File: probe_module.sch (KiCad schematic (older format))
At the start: 4 parts, among them J6 CONN_01X05, J7 CONN_01X05, U6 DG411, U7 LH1526

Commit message: Re-annotation
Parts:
- removed unit 1 of U6
- removed unit 3 of U6
- removed unit 4 of U6
- removed U7: LH1526, symbol LH1526
- added unit 1 of U5
- added unit 3 of U5
- added unit 4 of U5
- added U6: LH1526, symbol LH1526
- renumbered U6 to U5
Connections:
- net +3V3: now also U5.13 (V+), U5.13 (V+), U5.13 (V+)
- net GND: now also U5.4 (V-), U5.4 (V-), U5.4 (V-), U5.5 (GND), U5.5 (GND), U5.5 (GND), U6.2 (CTRL1_out), U6.4 (CTRL2_out)
- net VCC: now also U5.12 (VCC), U5.12 (VCC), U5.12 (VCC), U6.6 (S2), U6.8 (S1)
- net prb1_a: now also U5.3 (OUT)
- net prb1_pwr_ctrl: now also U6.1 (CTRL1_in)
- net prb1_rs_ctrl: now also U5.1 (SW)
- net prb1_v: now also U6.5 (S2')
- net prb2_a: now also U5.11 (OUT)
- net prb2_b: now also U5.15 (IN)
- net prb2_pwr_ctrl: now also U6.3 (CTRL2_in)
- net prb2_rs_ctrl: now also U5.16 (SW), U5.9 (SW)
- net prb2_v: now also U6.7 (S1')
- net vaisala_rs485_a: now also U5.10 (IN), U5.2 (IN)
- net vaisala_rs485_b: now also U5.14 (OUT)
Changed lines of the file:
@@
 $EndDescr
 $Comp
-L DG411 U6
-U 1 1 5981A21D
+L DG411 U5
+U 1 1 59945E5C
 P 2300 4450
-AR Path="/598183C5/5981A21D" Ref="U6"  Part="1"
-AR Path="/59933B07/5981A21D" Ref="U10"  Part="1"
-F 0 "U6" H 2300 4550 50  0000 C CNN
+F 0 "U5" H 2300 4550 50  0000 C CNN
 F 1 "DG411" H 2300 4350 50  0000 C CNN
 F 2 "" H 2300 4450 60  0001 C CNN
@@
 $EndComp
 $Comp
-L GND #PWR041
+L GND #PWR35
 U 1 1 5981A4AC
 P 2350 4950
-AR Path="/598183C5/5981A4AC" Ref="#PWR041"  Part="1"
-AR Path="/59933B07/5981A4AC" Ref="#PWR95"  Part="1"
-F 0 "#PWR041" H 2350 4700 50  0001 C CNN
+F 0 "#PWR35" H 2350 4700 50  0001 C CNN
 F 1 "GND" H 2350 4800 50  0000 C CNN
 F 2 "" H 2350 4950 50  0001 C CNN
@@
 $EndComp
 $Comp
-L GND #PWR042
+L GND #PWR38
 U 1 1 5981A5BD
 P 4700 4950
-AR Path="/598183C5/5981A5BD" Ref="#PWR042"  Part="1"
-AR Path="/59933B07/5981A5BD" Ref="#PWR98"  Part="1"
-F 0 "#PWR042" H 4700 4700 50  0001 C CNN
+F 0 "#PWR38" H 4700 4700 50  0001 C CNN
 F 1 "GND" H 4700 4800 50  0000 C CNN
 F 2 "" H 4700 4950 50  0001 C CNN
@@
 $EndComp
 $Comp
-L +3.3V #PWR043
+L +3.3V #PWR34
 U 1 1 5981A680
 P 2350 3950
-AR Path="/598183C5/5981A680" Ref="#PWR043"  Part="1"
-AR Path="/59933B07/5981A680" Ref="#PWR94"  Part="1"
-F 0 "#PWR043" H 2350 3800 50  0001 C CNN
+F 0 "#PWR34" H 2350 3800 50  0001 C CNN
 F 1 "+3.3V" H 2350 4090 50  0000 C CNN
 F 2 "" H 2350 3950 50  0001 C CNN
@@
 $EndComp
 $Comp
-L +3.3V #PWR044
+L +3.3V #PWR37
 U 1 1 5981A69E
 P 4700 3950
-AR Path="/598183C5/5981A69E" Ref="#PWR044"  Part="1"
-AR Path="/59933B07/5981A69E" Ref="#PWR97"  Part="1"
-F 0 "#PWR044" H 4700 3800 50  0001 C CNN
+F 0 "#PWR37" H 4700 3800 50  0001 C CNN
 F 1 "+3.3V" H 4700 4090 50  0000 C CNN
 F 2 "" H 4700 3950 50  0001 C CNN
@@
 prb1_b
 $Comp
-L DG411 U6
+L DG411 U5
 U 2 1 5981A26A
 P 4650 4450
-AR Path="/598183C5/5981A26A" Ref="U6"  Part="2"
-AR Path="/59933B07/5981A26A" Ref="U10"  Part="2"
-F 0 "U6" H 4650 4550 50  0000 C CNN
+F 0 "U5" H 4650 4550 50  0000 C CNN
 F 1 "DG411" H 4650 4350 50  0000 C CNN
 F 2 "" H 4650 4450 60  0001 C CNN
@@
 vaisala_rs485_b
 $Comp
-L DG411 U6
-U 3 1 5981EAC3
+L DG411 U5
+U 3 1 59945E6E
 P 7400 4450
-AR Path="/598183C5/5981EAC3" Ref="U6"  Part="3"
-AR Path="/59933B07/5981EAC3" Ref="U10"  Part="3"
-F 0 "U6" H 7400 4550 50  0000 C CNN
+F 0 "U5" H 7400 4550 50  0000 C CNN
 F 1 "DG411" H 7400 4350 50  0000 C CNN
 F 2 "" H 7400 4450 60  0001 C CNN
@@
 $EndComp
 $Comp
-L GND #PWR045
-U 1 1 5981EAC9
+L GND #PWR44
+U 1 1 59945E6F
 P 7450 4950
-AR Path="/598183C5/5981EAC9" Ref="#PWR045"  Part="1"
-AR Path="/59933B07/5981EAC9" Ref="#PWR104"  Part="1"
-F 0 "#PWR045" H 7450 4700 50  0001 C CNN
+F 0 "#PWR44" H 7450 4700 50  0001 C CNN
 F 1 "GND" H 7450 4800 50  0000 C CNN
 F 2 "" H 7450 4950 50  0001 C CNN
@@
 $EndComp
 $Comp
-L GND #PWR046
-U 1 1 5981EACF
+L GND #PWR47
+U 1 1 59945E70
 P 9500 4900
-AR Path="/598183C5/5981EACF" Ref="#PWR046"  Part="1"
-AR Path="/59933B07/5981EACF" Ref="#PWR107"  Part="1"
-F 0 "#PWR046" H 9500 4650 50  0001 C CNN
+F 0 "#PWR47" H 9500 4650 50  0001 C CNN
 F 1 "GND" H 9500 4750 50  0000 C CNN
 F 2 "" H 9500 4900 50  0001 C CNN
@@
 $EndComp
 $Comp
-L +3.3V #PWR047
-U 1 1 5981EAD5
+L +3.3V #PWR43
+U 1 1 59945E71
 P 7450 3950
-AR Path="/598183C5/5981EAD5" Ref="#PWR047"  Part="1"
-AR Path="/59933B07/5981EAD5" Ref="#PWR103"  Part="1"
-F 0 "#PWR047" H 7450 3800 50  0001 C CNN
+F 0 "#PWR43" H 7450 3800 50  0001 C CNN
 F 1 "+3.3V" H 7450 4090 50  0000 C CNN
 F 2 "" H 7450 3950 50  0001 C CNN
@@
 $EndComp
 $Comp
-L +3.3V #PWR048
-U 1 1 5981EADB
+L +3.3V #PWR46
+U 1 1 59945E72
 P 9500 3900
-AR Path="/598183C5/5981EADB" Ref="#PWR048"  Part="1"
-AR Path="/59933B07/5981EADB" Ref="#PWR106"  Part="1"
-F 0 "#PWR048" H 9500 3750 50  0001 C CNN
+F 0 "#PWR46" H 9500 3750 50  0001 C CNN
 F 1 "+3.3V" H 9500 4040 50  0000 C CNN
 F 2 "" H 9500 3900 50  0001 C CNN
@@
 prb2_b
 $Comp
-L DG411 U6
-U 4 1 5981EAE3
+L DG411 U5
+U 4 1 59945E73
 P 9450 4400
-AR Path="/598183C5/5981EAE3" Ref="U6"  Part="4"
-AR Path="/59933B07/5981EAE3" Ref="U10"  Part="4"
-F 0 "U6" H 9450 4500 50  0000 C CNN
+F 0 "U5" H 9450 4500 50  0000 C CNN
 F 1 "DG411" H 9450 4300 50  0000 C CNN
 F 2 "" H 9450 4400 60  0001 C CNN
@@
 $Comp
 L CONN_01X05 J6
-U 1 1 598215F3
+U 1 1 59945E74
 P 3100 1700
-AR Path="/598183C5/598215F3" Ref="J6"  Part="1"
-AR Path="/59933B07/598215F3" Ref="J9"  Part="1"
 F 0 "J6" H 3100 2000 50  0000 C CNN
 F 1 "CONN_01X05" V 3200 1700 50  0000 C CNN
@@
 U 1 1 59821868
 P 8000 1600
-AR Path="/598183C5/59821868" Ref="J7"  Part="1"
-AR Path="/59933B07/59821868" Ref="J10"  Part="1"
 F 0 "J7" H 8000 1900 50  0000 C CNN
 F 1 "CONN_01X05" V 8100 1600 50  0000 C CNN
@@
 NoConn ~ 8200 1800
 $Comp
-L GND #PWR049
+L GND #PWR40
 U 1 1 5990A260
 P 5350 2750
-AR Path="/598183C5/5990A260" Ref="#PWR049"  Part="1"
-AR Path="/59933B07/5990A260" Ref="#PWR100"  Part="1"
-F 0 "#PWR049" H 5350 2500 50  0001 C CNN
+F 0 "#PWR40" H 5350 2500 50  0001 C CNN
 F 1 "GND" H 5350 2600 50  0000 C CNN
 F 2 "" H 5350 2750 50  0001 C CNN
@@
 $EndComp
 $Comp
-L GND #PWR050
-U 1 1 5990A28D
+L GND #PWR42
+U 1 1 59945E8C
 P 5550 2750
-AR Path="/598183C5/5990A28D" Ref="#PWR050"  Part="1"
-AR Path="/59933B07/5990A28D" Ref="#PWR102"  Part="1"
-F 0 "#PWR050" H 5550 2500 50  0001 C CNN
+F 0 "#PWR42" H 5550 2500 50  0001 C CNN
 F 1 "GND" H 5550 2600 50  0000 C CNN
 F 2 "" H 5550 2750 50  0001 C CNN
@@
 prb2_a
 $Comp
-L GND #PWR051
-U 1 1 5990A7F8
+L GND #PWR45
+U 1 1 59945E8D
 P 7900 2150
-AR Path="/598183C5/5990A7F8" Ref="#PWR051"  Part="1"
-AR Path="/59933B07/5990A7F8" Ref="#PWR105"  Part="1"
-F 0 "#PWR051" H 7900 1900 50  0001 C CNN
+F 0 "#PWR45" H 7900 1900 50  0001 C CNN
 F 1 "GND" H 7900 2000 50  0000 C CNN
 F 2 "" H 7900 2150 50  0001 C CNN
@@
 $EndComp
 $Comp
-L GND #PWR052
+L GND #PWR36
 U 1 1 5990A9E7
 P 3000 2250
-AR Path="/598183C5/5990A9E7" Ref="#PWR052"  Part="1"
-AR Path="/59933B07/5990A9E7" Ref="#PWR96"  Part="1"
-F 0 "#PWR052" H 3000 2000 50  0001 C CNN
+F 0 "#PWR36" H 3000 2000 50  0001 C CNN
 F 1 "GND" H 3000 2100 50  0000 C CNN
 F 2 "" H 3000 2250 50  0001 C CNN
@@
 $EndComp
 $Comp
-L VCC #PWR053
-U 1 1 5990AB6A
+L VCC #PWR39
+U 1 1 59945E8F
 P 5250 1700
-AR Path="/598183C5/5990AB6A" Ref="#PWR053"  Part="1"
-AR Path="/59933B07/5990AB6A" Ref="#PWR99"  Part="1"
-F 0 "#PWR053" H 5250 1550 50  0001 C CNN
+F 0 "#PWR39" H 5250 1550 50  0001 C CNN
 F 1 "VCC" H 5250 1850 50  0000 C CNN
 F 2 "" H 5250 1700 50  0001 C CNN
@@
 $EndComp
 $Comp
-L VCC #PWR054
-U 1 1 5990AB9B
+L VCC #PWR41
+U 1 1 59945E90
 P 5450 1700
-AR Path="/598183C5/5990AB9B" Ref="#PWR054"  Part="1"
-AR Path="/59933B07/5990AB9B" Ref="#PWR101"  Part="1"
-F 0 "#PWR054" H 5450 1550 50  0001 C CNN
+F 0 "#PWR41" H 5450 1550 50  0001 C CNN
 F 1 "VCC" H 5450 1850 50  0000 C CNN
 F 2 "" H 5450 1700 50  0001 C CNN
@@
 prb2_v
 $Comp
-L LH1526 U7
-U 1 1 5992F278
+L LH1526 U6
+U 1 1 59945E91
 P 5700 2800
-AR Path="/598183C5/5992F278" Ref="U7"  Part="1"
-AR Path="/59933B07/5992F278" Ref="U11"  Part="1"
-F 0 "U7" H 5750 2900 60  0000 C CNN
+F 0 "U6" H 5750 2900 60  0000 C CNN
 F 1 "LH1526" H 5750 2750 60  0000 C CNN
 F 2 "" H 5750 2750 60  0001 C CNN

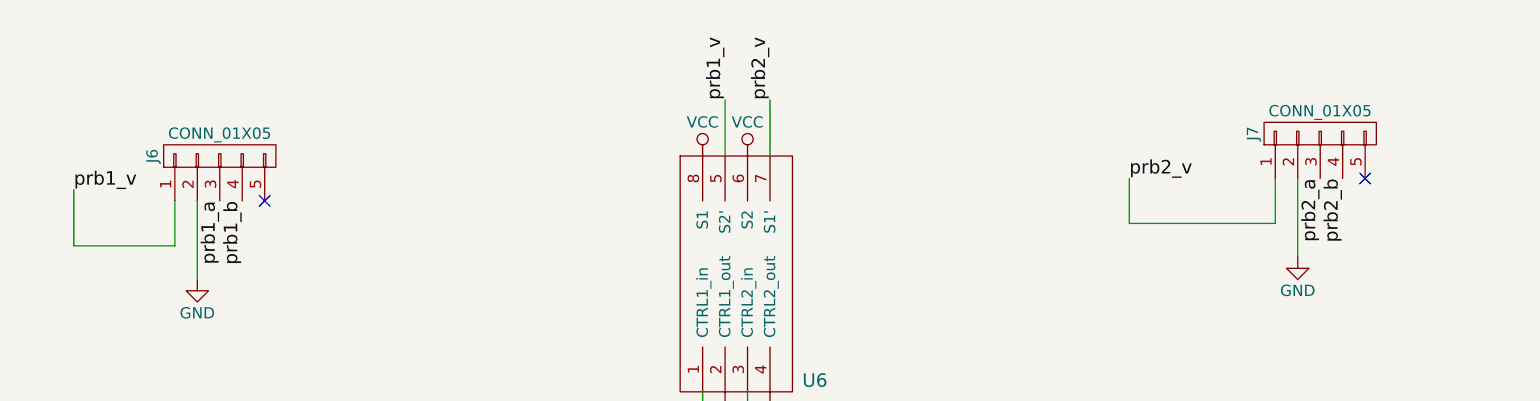
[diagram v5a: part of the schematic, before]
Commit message: add all the rest of the footprints
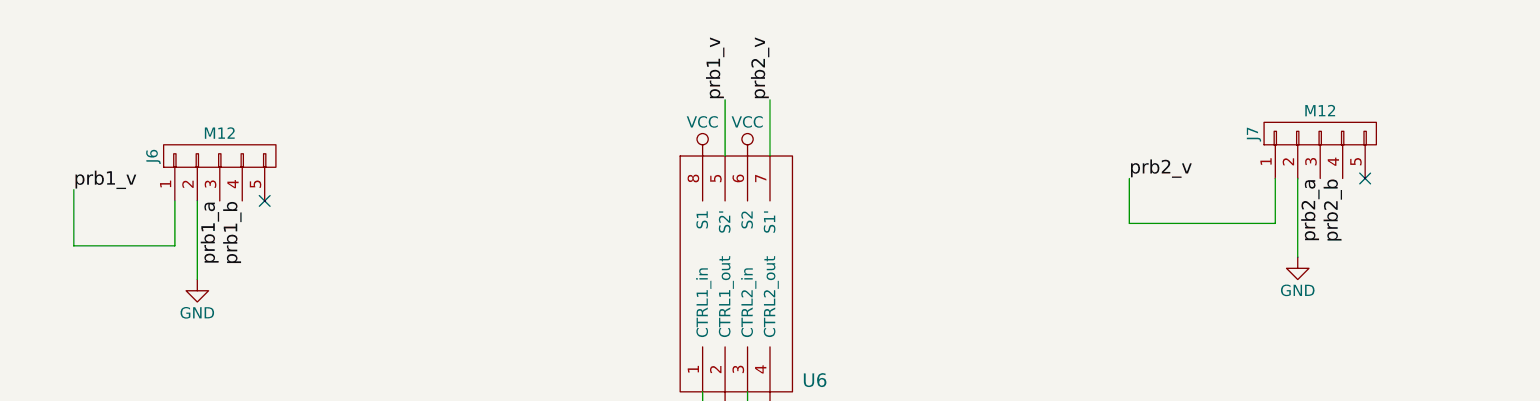
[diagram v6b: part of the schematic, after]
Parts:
- J6, J7: value CONN_01X05 -> M12; footprint (none) -> Connectors_Hirose:Hirose_DF13C-05P-1.25V_05x1.25mm_Straight
- U5: footprint (none) -> Housings_SOIC:SOIC-8_3.9x4.9mm_Pitch1.27mm
- U6: footprint (none) -> Housings_DIP:DIP-8_W9.53mm_SMD
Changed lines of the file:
@@
 F 0 "U5" H 2300 4550 50  0000 C CNN
 F 1 "DG411" H 2300 4350 50  0000 C CNN
-F 2 "" H 2300 4450 60  0001 C CNN
+F 2 "Housings_SOIC:SOIC-8_3.9x4.9mm_Pitch1.27mm" H 2300 4450 60  0001 C CNN
 F 3 "" H 2300 4450 60  0001 C CNN
 	1    2300 4450
@@
 F 0 "U5" H 4650 4550 50  0000 C CNN
 F 1 "DG411" H 4650 4350 50  0000 C CNN
-F 2 "" H 4650 4450 60  0001 C CNN
+F 2 "Housings_SOIC:SOIC-8_3.9x4.9mm_Pitch1.27mm" H 4650 4450 60  0001 C CNN
 F 3 "" H 4650 4450 60  0001 C CNN
 	2    4650 4450
@@
 F 0 "U5" H 7400 4550 50  0000 C CNN
 F 1 "DG411" H 7400 4350 50  0000 C CNN
-F 2 "" H 7400 4450 60  0001 C CNN
+F 2 "Housings_SOIC:SOIC-8_3.9x4.9mm_Pitch1.27mm" H 7400 4450 60  0001 C CNN
 F 3 "" H 7400 4450 60  0001 C CNN
 	3    7400 4450
@@
 F 0 "U5" H 9450 4500 50  0000 C CNN
 F 1 "DG411" H 9450 4300 50  0000 C CNN
-F 2 "" H 9450 4400 60  0001 C CNN
+F 2 "Housings_SOIC:SOIC-8_3.9x4.9mm_Pitch1.27mm" H 9450 4400 60  0001 C CNN
 F 3 "" H 9450 4400 60  0001 C CNN
 	4    9450 4400
@@
 P 3100 1700
 F 0 "J6" H 3100 2000 50  0000 C CNN
-F 1 "CONN_01X05" V 3200 1700 50  0000 C CNN
-F 2 "" H 3100 1700 50  0001 C CNN
+F 1 "M12" V 3200 1700 50  0000 C CNN
+F 2 "Connectors_Hirose:Hirose_DF13C-05P-1.25V_05x1.25mm_Straight" H 3100 1700 50  0001 C CNN
 F 3 "" H 3100 1700 50  0001 C CNN
 	1    3100 1700
@@
 P 8000 1600
 F 0 "J7" H 8000 1900 50  0000 C CNN
-F 1 "CONN_01X05" V 8100 1600 50  0000 C CNN
-F 2 "" H 8000 1600 50  0001 C CNN
+F 1 "M12" V 8100 1600 50  0000 C CNN
+F 2 "Connectors_Hirose:Hirose_DF13C-05P-1.25V_05x1.25mm_Straight" H 8000 1600 50  0001 C CNN
 F 3 "" H 8000 1600 50  0001 C CNN
 	1    8000 1600
@@
 F 0 "U6" H 5750 2900 60  0000 C CNN
 F 1 "LH1526" H 5750 2750 60  0000 C CNN
-F 2 "" H 5750 2750 60  0001 C CNN
+F 2 "Housings_DIP:DIP-8_W9.53mm_SMD" H 5750 2750 60  0001 C CNN
 F 3 "" H 5750 2750 60  0001 C CNN
 	1    5700 2800

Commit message: fix footprint errors
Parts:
- U5: footprint Housings_SOIC:SOIC-8_3.9x4.9mm_Pitch1.27mm -> Housings_DIP:DIP-16_W7.62mm_SMD
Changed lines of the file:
@@
 F 0 "U5" H 2300 4550 50  0000 C CNN
 F 1 "DG411" H 2300 4350 50  0000 C CNN
-F 2 "Housings_SOIC:SOIC-8_3.9x4.9mm_Pitch1.27mm" H 2300 4450 60  0001 C CNN
+F 2 "Housings_DIP:DIP-16_W7.62mm_SMD" H 2300 4450 60  0001 C CNN
 F 3 "" H 2300 4450 60  0001 C CNN
 	1    2300 4450
@@
 F 0 "U5" H 4650 4550 50  0000 C CNN
 F 1 "DG411" H 4650 4350 50  0000 C CNN
-F 2 "Housings_SOIC:SOIC-8_3.9x4.9mm_Pitch1.27mm" H 4650 4450 60  0001 C CNN
+F 2 "Housings_DIP:DIP-16_W7.62mm_SMD" H 4650 4450 60  0001 C CNN
 F 3 "" H 4650 4450 60  0001 C CNN
 	2    4650 4450
@@
 F 0 "U5" H 7400 4550 50  0000 C CNN
 F 1 "DG411" H 7400 4350 50  0000 C CNN
-F 2 "Housings_SOIC:SOIC-8_3.9x4.9mm_Pitch1.27mm" H 7400 4450 60  0001 C CNN
+F 2 "Housings_DIP:DIP-16_W7.62mm_SMD" H 7400 4450 60  0001 C CNN
 F 3 "" H 7400 4450 60  0001 C CNN
 	3    7400 4450
@@
 F 0 "U5" H 9450 4500 50  0000 C CNN
 F 1 "DG411" H 9450 4300 50  0000 C CNN
-F 2 "Housings_SOIC:SOIC-8_3.9x4.9mm_Pitch1.27mm" H 9450 4400 60  0001 C CNN
+F 2 "Housings_DIP:DIP-16_W7.62mm_SMD" H 9450 4400 60  0001 C CNN
 F 3 "" H 9450 4400 60  0001 C CNN
 	4    9450 4400
